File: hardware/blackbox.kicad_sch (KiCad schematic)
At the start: 3 parts

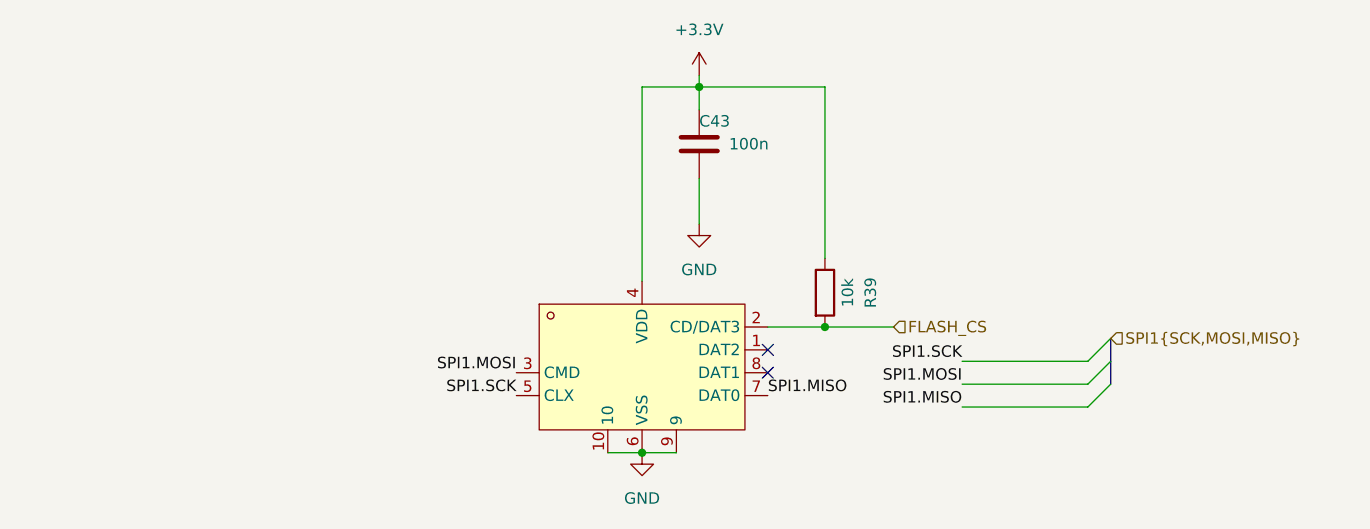
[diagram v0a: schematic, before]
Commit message: many tiny improvements
- I/O correctness
- SPI0/SPI1/I2C0 bus corrections
- decoupling of DVDD
- ADC_AVDD as per RPi documents
- removal of SBUS
- connect ESC serial
- remove RUN RC-circuit as per RPi documentation
- some more cleanup for readability
- gyro CLKIN decision
- I2C 4.7k pullup
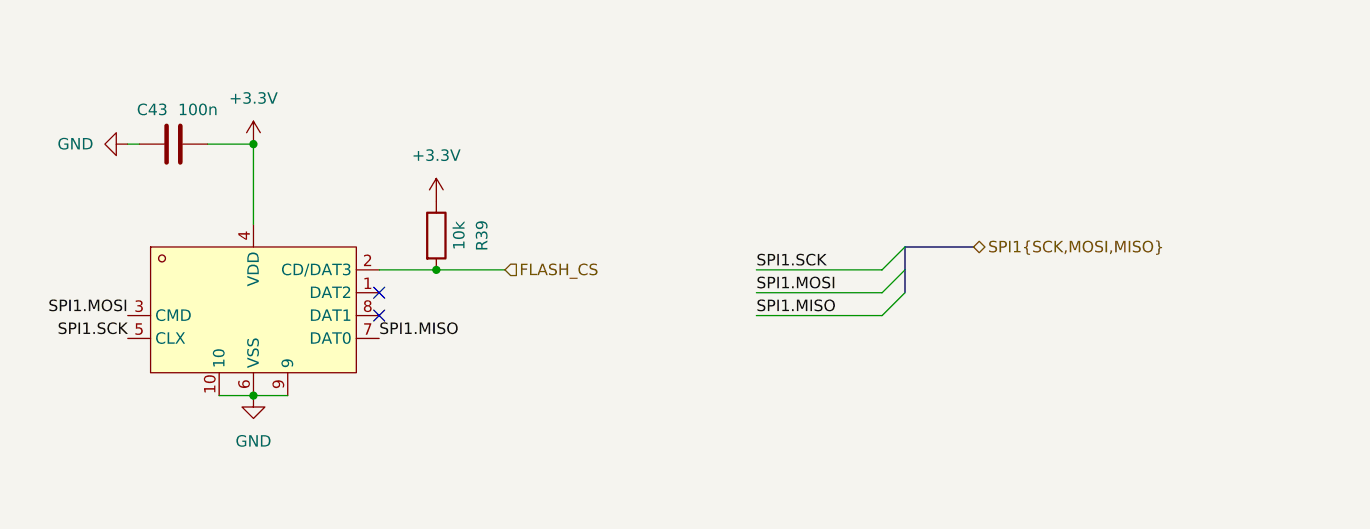
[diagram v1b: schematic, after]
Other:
- moved on the sheet: C43, R39
